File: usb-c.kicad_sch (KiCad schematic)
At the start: 14 parts, among them IC1 USBLC6-2SC6, IC2 632723100011, IC3 TCPP01-M12, Q1 STL11N3LLH6

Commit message: Components reindexing and update of PCB
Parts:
- renumbered C3 to C1, C1 to C2, C4 to C3, C2 to C4, D2 to D1, D1 to D2, IC2 to IC1, IC3 to IC2, IC1 to IC3
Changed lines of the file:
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@@
 		(dnp no)
 		(fields_autoplaced yes)
-		(property "Reference" "IC2"
+		(property "Reference" "IC1"
 			(at 97.79 58.42 0)
 			(effects
@@
 			(project "weather-station-poc"
 				(path "/38eb53bb-294e-46e4-ad59-fd355ca373b9/336d3e95-9b5f-4d37-8b5a-efff814cf96e"
-					(reference "IC2")
+					(reference "IC1")
 					(unit 1)
 				)
@@
 		(dnp no)
 		(fields_autoplaced yes)
-		(property "Reference" "C4"
+		(property "Reference" "C3"
 			(at 222.25 83.8199 0)
 			(effects
@@
 			(project "weather-station-poc"
 				(path "/38eb53bb-294e-46e4-ad59-fd355ca373b9/336d3e95-9b5f-4d37-8b5a-efff814cf96e"
-					(reference "C4")
+					(reference "C3")
 					(unit 1)
 				)
@@
 		(dnp no)
 		(fields_autoplaced yes)
-		(property "Reference" "#PWR011"
+		(property "Reference" "#PWR020"
 			(at 73.66 128.27 0)
 			(effects
@@
 			(project "weather-station-poc"
 				(path "/38eb53bb-294e-46e4-ad59-fd355ca373b9/336d3e95-9b5f-4d37-8b5a-efff814cf96e"
-					(reference "#PWR011")
+					(reference "#PWR020")
 					(unit 1)
 				)
@@
 		(on_board yes)
 		(dnp no)
-		(property "Reference" "D2"
+		(property "Reference" "D1"
 			(at 150.114 77.978 90)
 			(effects
@@
 			(project ""
 				(path "/38eb53bb-294e-46e4-ad59-fd355ca373b9/336d3e95-9b5f-4d37-8b5a-efff814cf96e"
-					(reference "D2")
+					(reference "D1")
 					(unit 1)
 				)
@@
 		(dnp no)
 		(fields_autoplaced yes)
-		(property "Reference" "C3"
+		(property "Reference" "C1"
 			(at 171.45 72.3899 0)
 			(effects
@@
 			(project "weather-station-poc"
 				(path "/38eb53bb-294e-46e4-ad59-fd355ca373b9/336d3e95-9b5f-4d37-8b5a-efff814cf96e"
-					(reference "C3")
+					(reference "C1")
 					(unit 1)
 				)
@@
 		(dnp no)
 		(fields_autoplaced yes)
-		(property "Reference" "#PWR019"
+		(property "Reference" "#PWR015"
 			(at 201.93 109.22 0)
 			(effects
@@
 			(project "weather-station-poc"
 				(path "/38eb53bb-294e-46e4-ad59-fd355ca373b9/336d3e95-9b5f-4d37-8b5a-efff814cf96e"
-					(reference "#PWR019")
+					(reference "#PWR015")
 					(unit 1)
 				)
@@
 		(dnp no)
 		(fields_autoplaced yes)
-		(property "Reference" "#PWR020"
+		(property "Reference" "#PWR012"
 			(at 218.44 95.25 0)
 			(effects
@@
 			(project "weather-station-poc"
 				(path "/38eb53bb-294e-46e4-ad59-fd355ca373b9/336d3e95-9b5f-4d37-8b5a-efff814cf96e"
-					(reference "#PWR020")
+					(reference "#PWR012")
 					(unit 1)
 				)
@@
 		(dnp no)
 		(fields_autoplaced yes)
-		(property "Reference" "C2"
+		(property "Reference" "C4"
 			(at 160.02 113.0299 0)
 			(effects
@@
 			(project "weather-station-poc"
 				(path "/38eb53bb-294e-46e4-ad59-fd355ca373b9/336d3e95-9b5f-4d37-8b5a-efff814cf96e"
-					(reference "C2")
+					(reference "C4")
 					(unit 1)
 				)
@@
 		(on_board yes)
 		(dnp no)
-		(property "Reference" "IC3"
+		(property "Reference" "IC2"
 			(at 192.786 91.694 0)
 			(effects
@@
 			(project "weather-station-poc"
 				(path "/38eb53bb-294e-46e4-ad59-fd355ca373b9/336d3e95-9b5f-4d37-8b5a-efff814cf96e"
-					(reference "IC3")
+					(reference "IC2")
 					(unit 1)
 				)
@@
 		(dnp no)
 		(fields_autoplaced yes)
-		(property "Reference" "#PWR013"
+		(property "Reference" "#PWR011"
 			(at 120.65 83.82 0)
 			(effects
@@
 			(project "weather-station-poc"
 				(path "/38eb53bb-294e-46e4-ad59-fd355ca373b9/336d3e95-9b5f-4d37-8b5a-efff814cf96e"
-					(reference "#PWR013")
+					(reference "#PWR011")
 					(unit 1)
 				)
@@
 		(dnp no)
 		(fields_autoplaced yes)
-		(property "Reference" "#PWR014"
+		(property "Reference" "#PWR017"
 			(at 156.21 124.46 0)
 			(effects
@@
 			(project "weather-station-poc"
 				(path "/38eb53bb-294e-46e4-ad59-fd355ca373b9/336d3e95-9b5f-4d37-8b5a-efff814cf96e"
-					(reference "#PWR014")
+					(reference "#PWR017")
 					(unit 1)
 				)
@@
 		(on_board yes)
 		(dnp no)
-		(property "Reference" "#PWR015"
+		(property "Reference" "#PWR014"
 			(at 157.48 101.6 0)
 			(effects
@@
 			(project "weather-station-poc"
 				(path "/38eb53bb-294e-46e4-ad59-fd355ca373b9/336d3e95-9b5f-4d37-8b5a-efff814cf96e"
-					(reference "#PWR015")
+					(reference "#PWR014")
 					(unit 1)
 				)
@@
 		(dnp no)
 		(fields_autoplaced yes)
-		(property "Reference" "#PWR017"
+		(property "Reference" "#PWR019"
 			(at 177.8 130.81 0)
 			(effects
@@
 			(project "weather-station-poc"
 				(path "/38eb53bb-294e-46e4-ad59-fd355ca373b9/336d3e95-9b5f-4d37-8b5a-efff814cf96e"
-					(reference "#PWR017")
+					(reference "#PWR019")
 					(unit 1)
 				)
@@
 		(dnp no)
 		(fields_autoplaced yes)
-		(property "Reference" "D1"
+		(property "Reference" "D2"
 			(at 143.51 100.33 0)
 			(effects
@@
 			(project ""
 				(path "/38eb53bb-294e-46e4-ad59-fd355ca373b9/336d3e95-9b5f-4d37-8b5a-efff814cf96e"
-					(reference "D1")
+					(reference "D2")
 					(unit 1)
 				)
@@
 		(dnp no)
 		(fields_autoplaced yes)
-		(property "Reference" "C1"
+		(property "Reference" "C2"
 			(at 140.97 78.7399 0)
 			(effects
@@
 			(project "weather-station-poc"
 				(path "/38eb53bb-294e-46e4-ad59-fd355ca373b9/336d3e95-9b5f-4d37-8b5a-efff814cf96e"
-					(reference "C1")
+					(reference "C2")
 					(unit 1)
 				)
@@
 		(dnp no)
 		(fields_autoplaced yes)
-		(property "Reference" "#PWR012"
+		(property "Reference" "#PWR013"
 			(at 74.93 93.98 0)
 			(effects
@@
 			(project "weather-station-poc"
 				(path "/38eb53bb-294e-46e4-ad59-fd355ca373b9/336d3e95-9b5f-4d37-8b5a-efff814cf96e"
-					(reference "#PWR012")
+					(reference "#PWR013")
 					(unit 1)
 				)
@@
 		(dnp no)
 		(fields_autoplaced yes)
-		(property "Reference" "#PWR018"
+		(property "Reference" "#PWR016"
 			(at 190.5 115.57 0)
 			(effects
@@
 			(project "weather-station-poc"
 				(path "/38eb53bb-294e-46e4-ad59-fd355ca373b9/336d3e95-9b5f-4d37-8b5a-efff814cf96e"
-					(reference "#PWR018")
+					(reference "#PWR016")
 					(unit 1)
 				)
@@
 		(dnp no)
 		(fields_autoplaced yes)
-		(property "Reference" "IC1"
+		(property "Reference" "IC3"
 			(at 96.52 118.11 0)
 			(effects
@@
 			(project "weather-station-poc"
 				(path "/38eb53bb-294e-46e4-ad59-fd355ca373b9/336d3e95-9b5f-4d37-8b5a-efff814cf96e"
-					(reference "IC1")
+					(reference "IC3")
 					(unit 1)
 				)
@@
 		(dnp no)
 		(fields_autoplaced yes)
-		(property "Reference" "#PWR016"
+		(property "Reference" "#PWR018"
 			(at 172.72 130.81 0)
 			(effects
@@
 			(project "weather-station-poc"
 				(path "/38eb53bb-294e-46e4-ad59-fd355ca373b9/336d3e95-9b5f-4d37-8b5a-efff814cf96e"
-					(reference "#PWR016")
-					(unit 1)
-				)
+					(reference "#PWR018")
+					(unit 1)
+				)

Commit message: Add 3V3 copper pour on L1 and connect to nets
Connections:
- net VBUS: no longer IC1.A4 (VBUS_1), IC1.A9 (VBUS_2)
- no-connect marks 11 -> 13
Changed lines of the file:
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@@
+	)
+	(no_connect
+		(at 81.28 86.36)
 	)
 	(no_connect
@@
 	(no_connect
 		(at 81.28 91.44)
+	)
+	(no_connect
+		(at 81.28 73.66)
 	)
 	(no_connect
@@
 		)
 	)
-	(label "VBUS"
-		(at 81.28 73.66 180)
-		(effects
-			(font
-				(size 1.27 1.27)
-			)
-			(justify right bottom)
-		)
-	)
 	(label "CC1c"
 		(at 162.56 104.14 180)
@@
 		)
 	)
-	(label "VBUS"
-		(at 81.28 86.36 180)
-		(effects
-			(font
-				(size 1.27 1.27)
-			)
-			(justify right bottom)
-		)
-	)

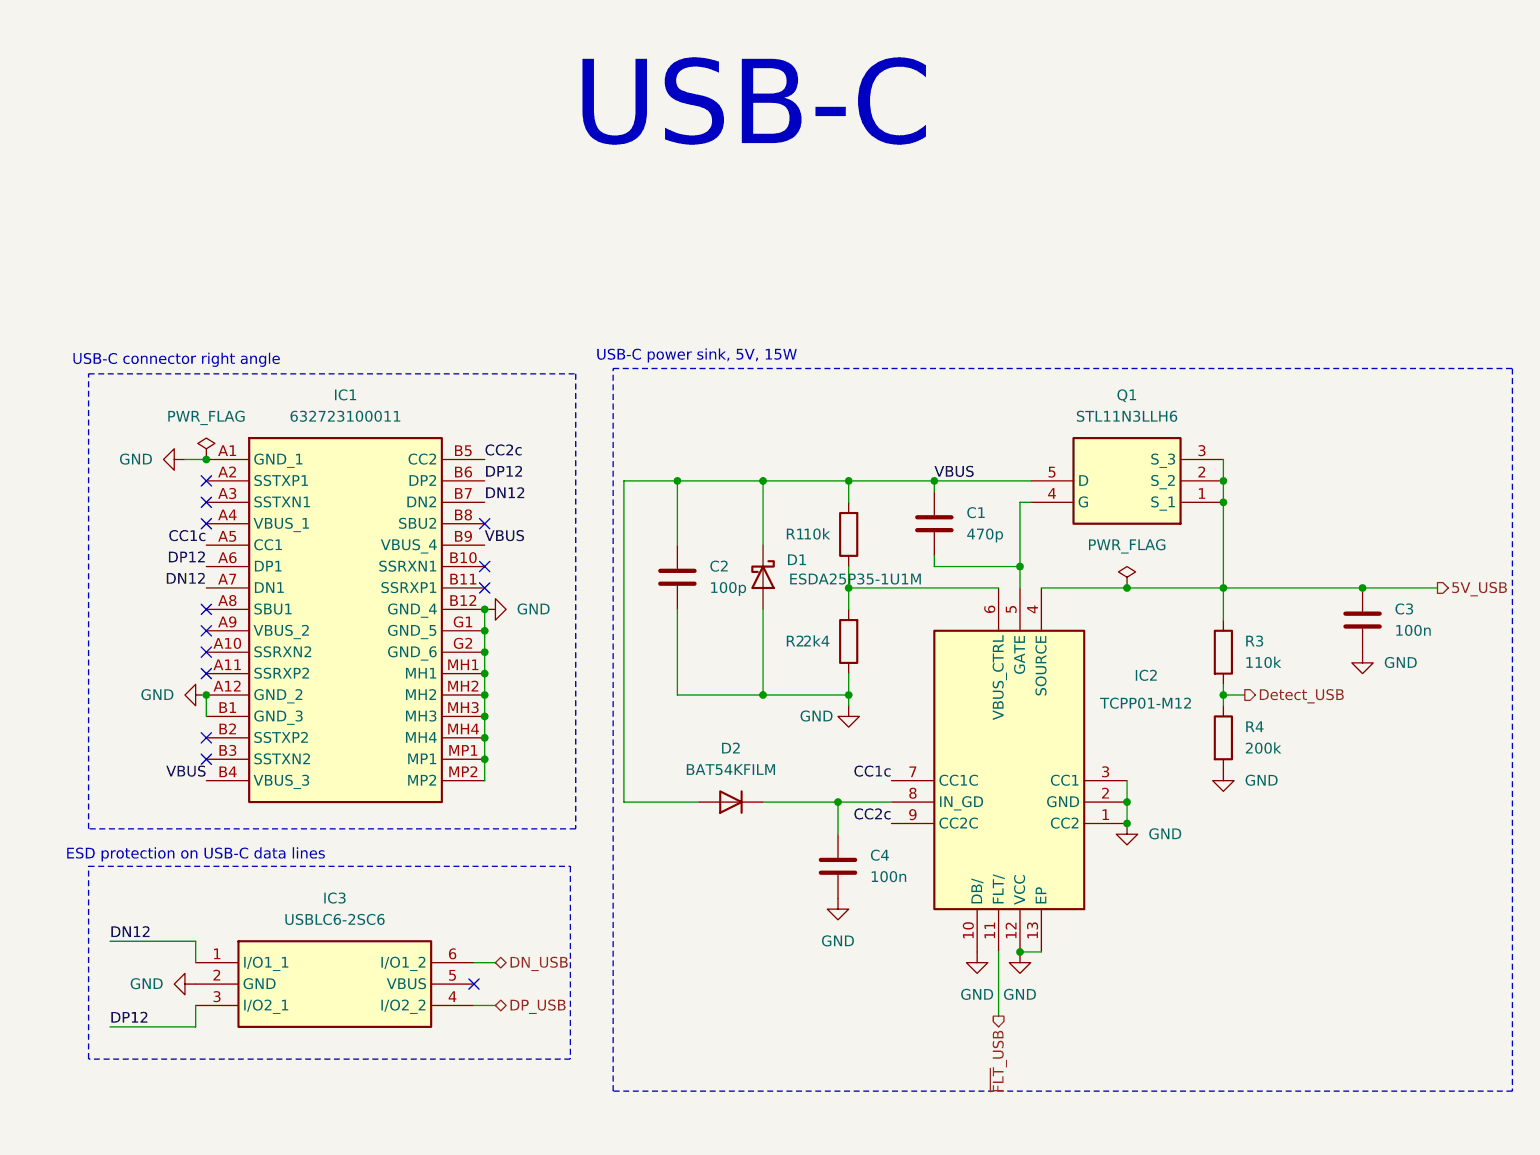
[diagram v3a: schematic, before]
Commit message: Update schematic to Kicad 10
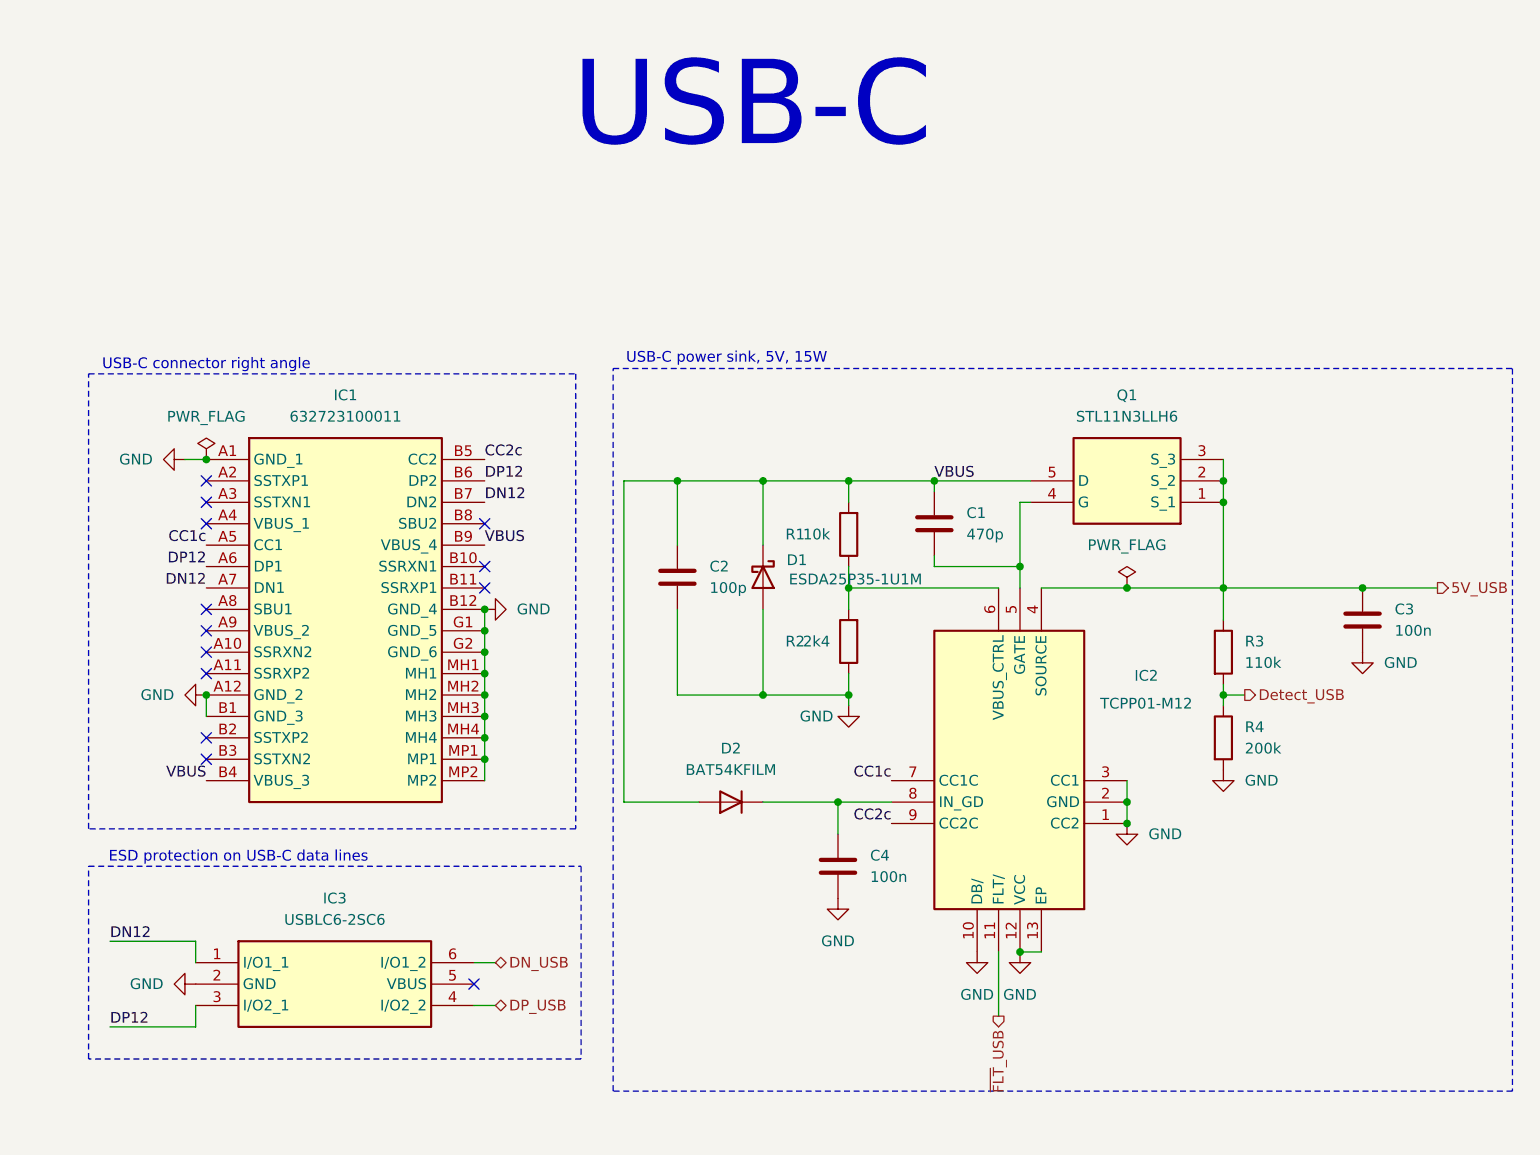
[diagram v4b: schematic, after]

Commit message: Add tests points with 5015 footprint for practicity
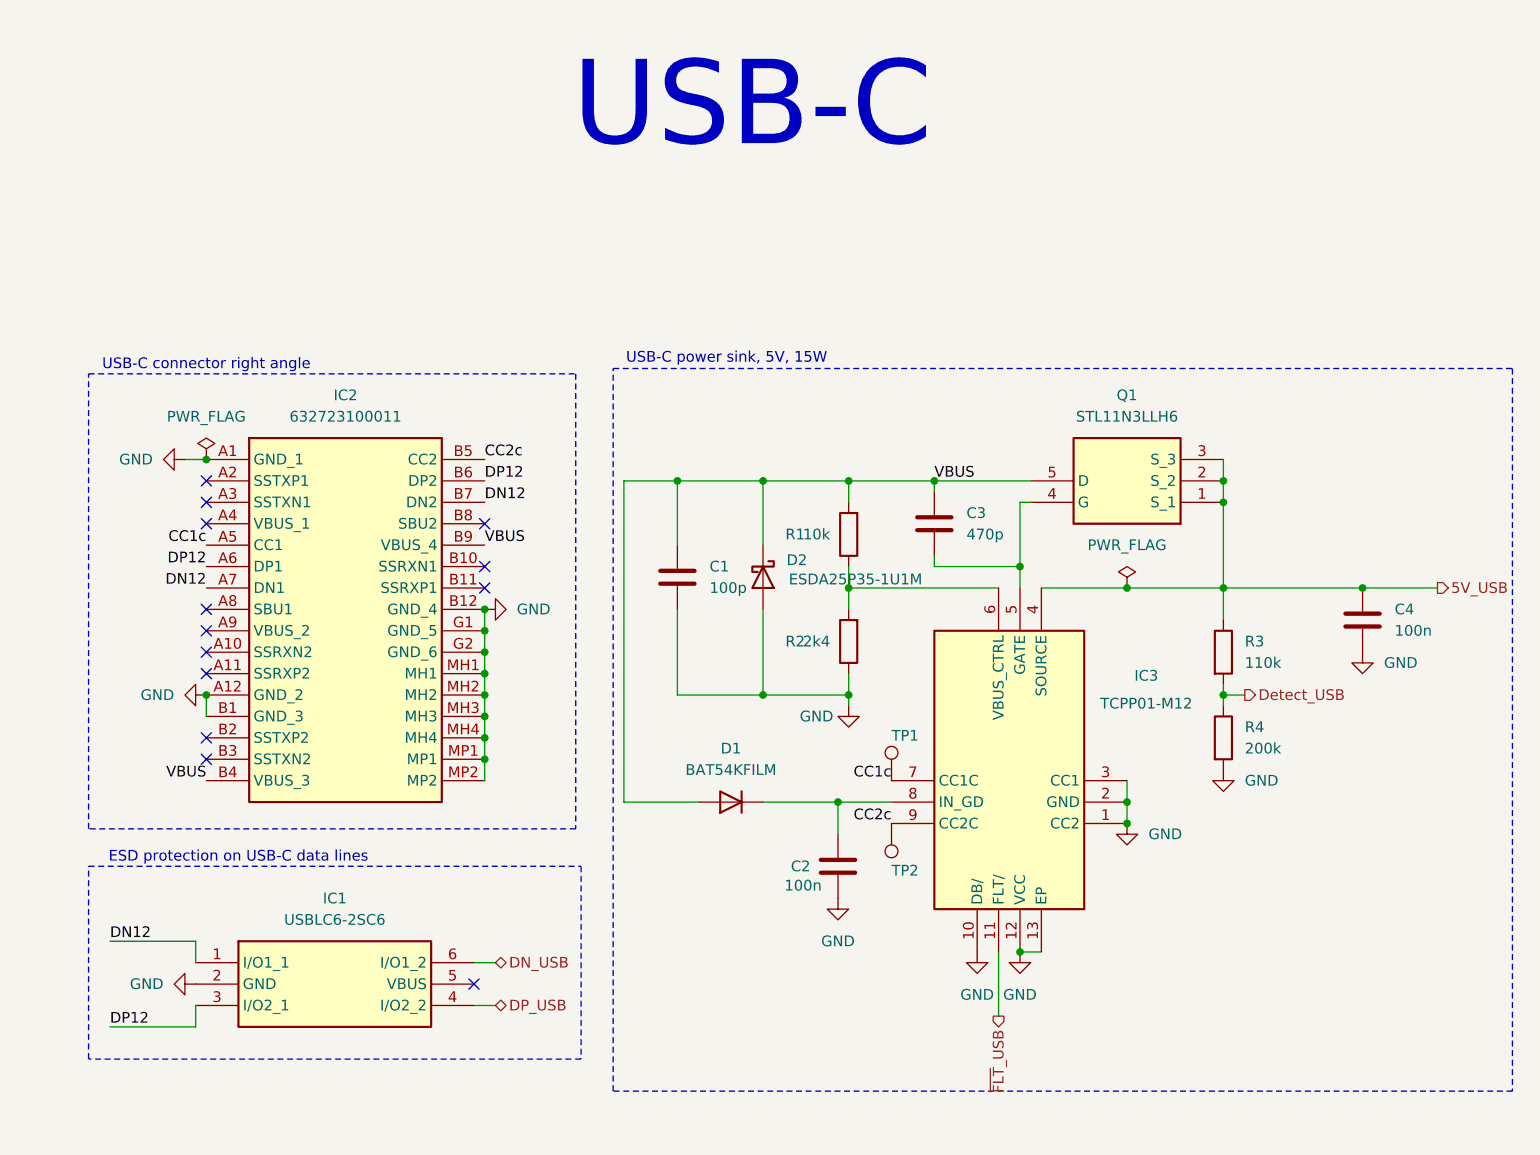
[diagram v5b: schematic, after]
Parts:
- added TP1, TP2: TestPoint, weather-station-poc-fp:5015, symbol Connector:TestPoint
- renumbered C2 to C1, C4 to C2, C1 to C3, C3 to C4, D2 to D1, D1 to D2, IC3 to IC1, IC1 to IC2, IC2 to IC3
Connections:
- net CC1c: now also TP1.1
- net CC2c: now also TP2.1

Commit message: Complete all references for components
Modifgy Y1 and Y2 capacitors footprint from 0603 to 0402
Modify footprint of SWD connector
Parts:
- C1: Manufacturer_Name (none) -> Wurth Elektronik; Manufacturer_Part_Number (none) -> 885012206003
- C2, C4: Manufacturer_Name (none) -> Wurth Elektronik; Manufacturer_Part_Number (none) -> 885012206020
- C3: Manufacturer_Name (none) -> Wurth Elektronik; Manufacturer_Part_Number (none) -> 885012206006
- R1: Manufacturer_Name (none) -> Wurth Elektronik; Manufacturer_Part_Number (none) -> 560112116005
- R2: Manufacturer_Name (none) -> Wurth Elektronik; Manufacturer_Part_Number (none) -> 560112116061
- R3: Manufacturer_Name (none) -> Wurth Elektronik; Manufacturer_Part_Number (none) -> 560112116148
- R4: Manufacturer_Name (none) -> Wurth Elektronik; Manufacturer_Part_Number (none) -> 560112116060
- TP1, TP2: Manufacturer_Name (none) -> N/A; Manufacturer_Part_Number (none) -> N/A
